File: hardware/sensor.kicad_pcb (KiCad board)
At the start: 2 copper layers, 29 x 31 mm, 56 parts, among them P1 CONN_01X05, SW1 Reset, T1 BUK9Y22, U1 LMR16006, U2 CD74HC4046, U3 CD74HC4046, U4 Atmel_SAM_D09, U5 OPA376AIDCK, X1 UART, X2 60V

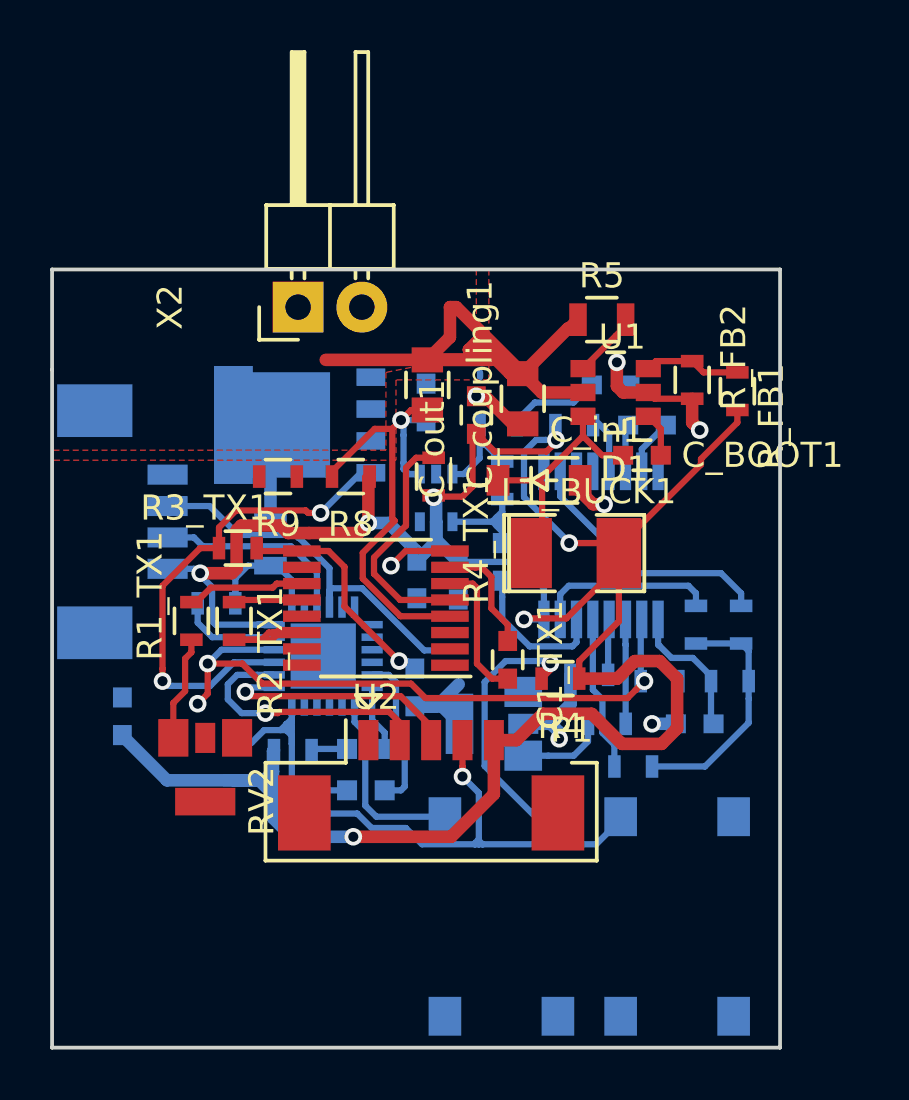
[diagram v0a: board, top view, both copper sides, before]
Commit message: Done routing. Some DRC fails but that should be ok!
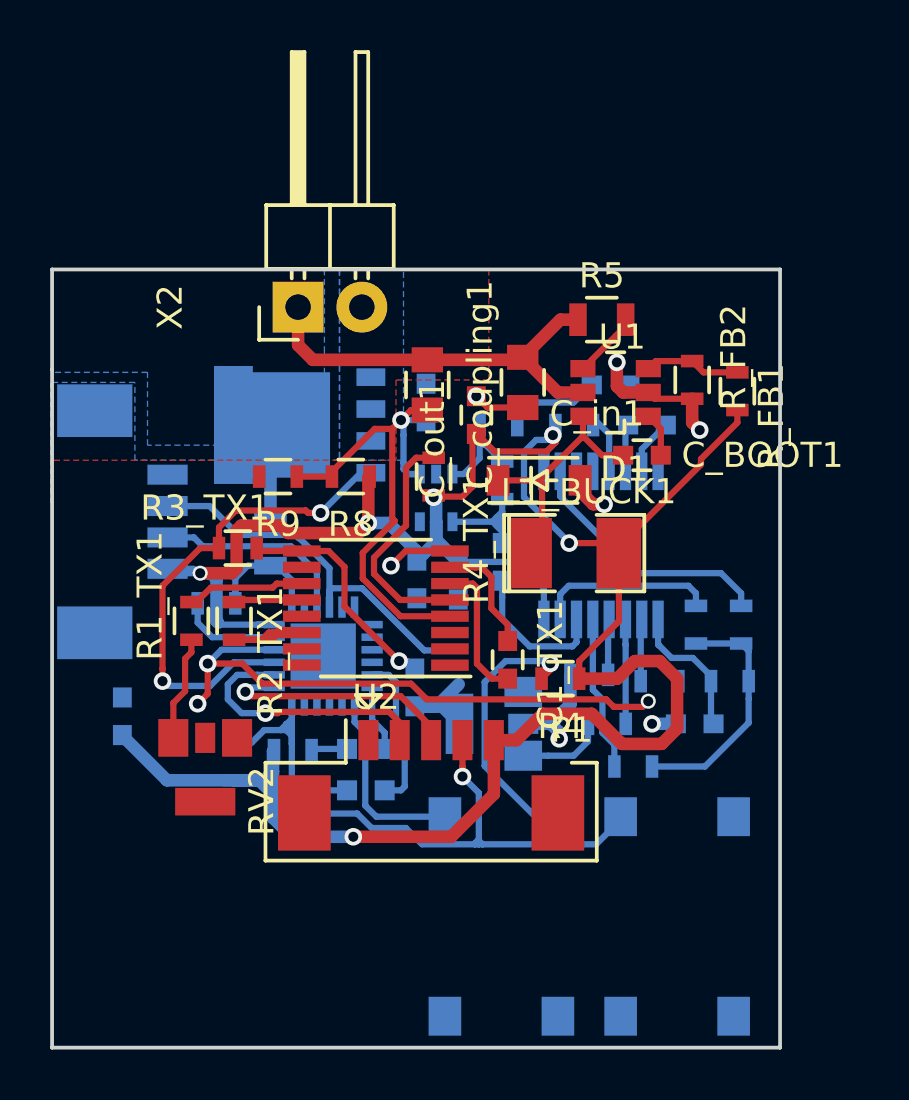
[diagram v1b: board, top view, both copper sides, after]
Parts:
- moved C_in1 0.65 mm to (162.8, 79.5)
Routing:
- net VCC: track 29.9 -> 21.0 mm
- net +3V3: track 106.1 -> 102.2 mm, vias 7 -> 6
- net /coupling: track 19.8 -> 21.2 mm
- added copper zone on B.Cu, net VCC
- removed copper zone on F.Cu, net VCC

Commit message: Bottom layer labels arranged
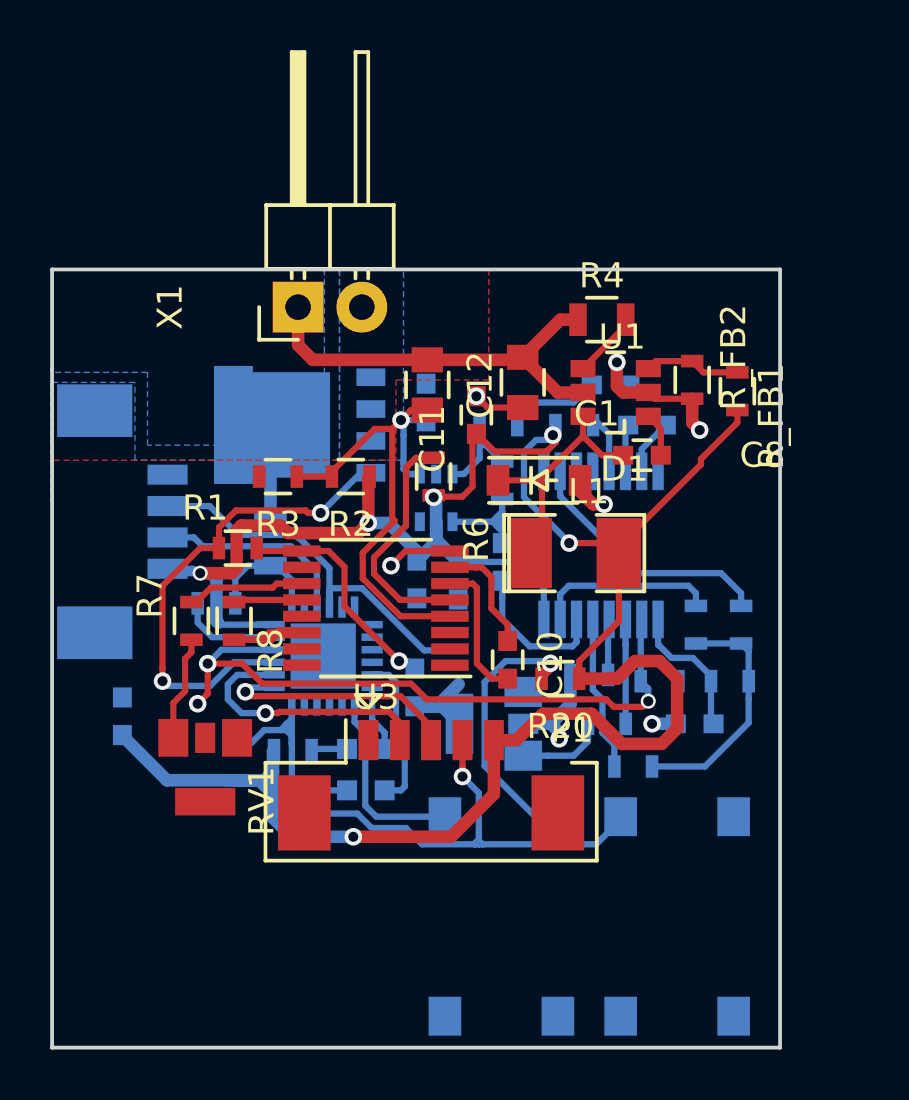
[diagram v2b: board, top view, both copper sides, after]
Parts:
- renumbered C_in1 to C1, C1_TX1 to C10, C_out1 to C11, C_coupling1 to C12, C1_RX1 to C13, C6 to C14, C1 to C2, C2_TX1 to C3, C2 to C4, C3 to C5, C4 to C6, C2_RX1 to C7, C_BOOT1 to C8, C5 to C9, L1_BUCK1 to L1, R3_TX1 to R1, R11 to R10, R4_RX1 to R11, R1_RX1 to R12, R2_RX1 to R13, R5_RX1 to R14, R1 to R15, R6 to R16, R7 to R17, R2 to R18, R3 to R19, R8 to R2, R4 to R20, R9 to R3, R5 to R4, R10 to R5, R4_TX1 to R6, R1_TX1 to R7, R2_TX1 to R8, R3_RX1 to R9, RV2 to RV1, RV1 to RV2, U5 to U2, U2 to U3, U3 to U4, U4 to U5, X2 to X1, X1 to X2
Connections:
- P1 pad : GND -> (no net)
- RV1 pad 4: GND -> (no net)
- RV2 pad 4: GND -> (no net)
- X2 pad : GND -> (no net)
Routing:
- net /RX1_out: track 25.5 -> 26.4 mm
